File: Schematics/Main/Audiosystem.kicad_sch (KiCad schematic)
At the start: 2 parts

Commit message: Added potentiometer and loudspeakers to audio schematic
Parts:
- added RV1: 2 kΩ, symbol Device:R_Potentiometer_Dual
- R10, R11: value 1 MΩ -> 220 kΩ
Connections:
- net LOUT-: now also RV1.6
- net ROUT-: now also RV1.1
- new net PAM8403-Board/LOUT-: RV1.4
- new net PAM8403-Board/ROUT-: RV1.3
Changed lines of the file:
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@@
 	(wire
 		(pts
-			(xy 176.53 114.3) (xy 186.69 114.3)
+			(xy 203.2 102.87) (xy 215.9 102.87)
 		)
 		(stroke
@@
 	(wire
 		(pts
+			(xy 203.2 114.3) (xy 176.53 114.3)
+		)
+		(stroke
+			(width 0)
+			(type default)
+		)
+	)
+	(wire
+		(pts
+			(xy 187.96 123.19) (xy 187.96 125.73)
+		)
+		(stroke
+			(width 0)
+			(type default)
+		)
+	)
+	(wire
+		(pts
 			(xy 105.41 107.95) (xy 105.41 104.14)
 		)
@@
 	(wire
 		(pts
+			(xy 205.74 135.89) (xy 215.9 135.89)
+		)
+		(stroke
+			(width 0)
+			(type default)
+		)
+	)
+	(wire
+		(pts
 			(xy 143.51 114.3) (xy 148.59 114.3)
 		)
@@
 	(wire
 		(pts
-			(xy 176.53 116.84) (xy 186.69 116.84)
-		)
-		(stroke
-			(width 0)
-			(type default)
-		)
-	)
-	(wire
-		(pts
 			(xy 100.33 104.14) (xy 97.79 104.14)
 		)
@@
 	(wire
 		(pts
+			(xy 187.96 125.73) (xy 176.53 125.73)
+		)
+		(stroke
+			(width 0)
+			(type default)
+		)
+	)
+	(wire
+		(pts
 			(xy 76.2 127) (xy 80.01 127)
 		)
@@
 	(wire
 		(pts
+			(xy 205.74 110.49) (xy 205.74 106.68)
+		)
+		(stroke
+			(width 0)
+			(type default)
+		)
+	)
+	(wire
+		(pts
+			(xy 205.74 130.81) (xy 205.74 135.89)
+		)
+		(stroke
+			(width 0)
+			(type default)
+		)
+	)
+	(wire
+		(pts
+			(xy 203.2 139.7) (xy 203.2 128.27)
+		)
+		(stroke
+			(width 0)
+			(type default)
+		)
+	)
+	(wire
+		(pts
 			(xy 100.33 101.6) (xy 100.33 104.14)
 		)
@@
 	(wire
 		(pts
+			(xy 203.2 128.27) (xy 176.53 128.27)
+		)
+		(stroke
+			(width 0)
+			(type default)
+		)
+	)
+	(wire
+		(pts
+			(xy 205.74 123.19) (xy 187.96 123.19)
+		)
+		(stroke
+			(width 0)
+			(type default)
+		)
+	)
+	(wire
+		(pts
 			(xy 62.23 119.38) (xy 80.01 119.38)
 		)
@@
 	(wire
 		(pts
+			(xy 203.2 102.87) (xy 203.2 114.3)
+		)
+		(stroke
+			(width 0)
+			(type default)
+		)
+	)
+	(wire
+		(pts
 			(xy 62.23 114.3) (xy 80.01 114.3)
 		)
@@
 	(wire
 		(pts
-			(xy 176.53 128.27) (xy 186.69 128.27)
+			(xy 203.2 139.7) (xy 215.9 139.7)
 		)
 		(stroke
@@
 	(wire
 		(pts
-			(xy 176.53 125.73) (xy 186.69 125.73)
-		)
-		(stroke
-			(width 0)
-			(type default)
-		)
-	)
-	(wire
-		(pts
 			(xy 137.16 128.27) (xy 148.59 128.27)
 		)
@@
 	(wire
 		(pts
+			(xy 187.96 116.84) (xy 176.53 116.84)
+		)
+		(stroke
+			(width 0)
+			(type default)
+		)
+	)
+	(wire
+		(pts
+			(xy 187.96 118.11) (xy 205.74 118.11)
+		)
+		(stroke
+			(width 0)
+			(type default)
+		)
+	)
+	(wire
+		(pts
 			(xy 60.96 92.71) (xy 66.04 92.71)
 		)
@@
 	(wire
 		(pts
+			(xy 205.74 106.68) (xy 215.9 106.68)
+		)
+		(stroke
+			(width 0)
+			(type default)
+		)
+	)
+	(wire
+		(pts
 			(xy 76.2 121.92) (xy 80.01 121.92)
+		)
+		(stroke
+			(width 0)
+			(type default)
+		)
+	)
+	(wire
+		(pts
+			(xy 187.96 118.11) (xy 187.96 116.84)
 		)
 		(stroke
@@
 	(hierarchical_label "ROUT-"
 		(shape output)
-		(at 186.69 116.84 0)
+		(at 215.9 106.68 0)
 		(effects
 			(font
@@
 	(hierarchical_label "LOUT+"
 		(shape output)
-		(at 186.69 128.27 0)
+		(at 215.9 139.7 0)
 		(effects
 			(font
@@
 	(hierarchical_label "LOUT-"
 		(shape output)
-		(at 186.69 125.73 0)
+		(at 215.9 135.89 0)
 		(effects
 			(font
@@
 	(hierarchical_label "ROUT+"
 		(shape output)
-		(at 186.69 114.3 0)
+		(at 215.9 102.87 0)
 		(effects
 			(font
@@
 			)
 		)
-		(property "Value" "1 MΩ"
+		(property "Value" "220 kΩ"
 			(at 133.35 119.38 90)
 			(effects
@@
 				(path "/2b6c83b8-b6db-46e9-a845-f7ffa0649aa2/64921ae5-eabb-49e5-933f-c558e83970f3"
 					(reference "#PWR042")
+					(unit 1)
+				)
+			)
+		)
+	)
+	(symbol
+		(lib_id "Device:R_Potentiometer_Dual")
+		(at 208.28 120.65 270)
+		(unit 1)
+		(exclude_from_sim no)
+		(in_bom yes)
+		(on_board yes)
+		(dnp no)
+		(fields_autoplaced yes)
+		(property "Reference" "RV1"
+			(at 203.2 119.3799 90)
+			(effects
+				(font
+					(size 1.27 1.27)
+				)
+				(justify right)
+			)
+		)
+		(property "Value" "2 kΩ"
+			(at 203.2 121.9199 90)
+			(effects
+				(font
+					(size 1.27 1.27)
+				)
+				(justify right)
+			)
+		)
+		(property "Footprint" ""
+			(at 206.375 127 0)
+			(effects
+				(font
+					(size 1.27 1.27)
+				)
+				(hide yes)
+			)
+		)
+		(property "Datasheet" "~"
+			(at 206.375 127 0)
+			(effects
+				(font
+					(size 1.27 1.27)
+				)
+				(hide yes)
+			)
+		)
+		(property "Description" "Dual potentiometer"
+			(at 208.28 120.65 0)
+			(effects
+				(font
+					(size 1.27 1.27)
+				)
+				(hide yes)
+			)
+		)
+		(pin "4"
+		)
+		(pin "3"
+		)
+		(pin "1"
+		)
+		(pin "5"
+		)
+		(pin "2"
+		)
+		(pin "6"
+		)
+		(instances
+			(project ""
+				(path "/2b6c83b8-b6db-46e9-a845-f7ffa0649aa2/64921ae5-eabb-49e5-933f-c558e83970f3"
+					(reference "RV1")
 					(unit 1)
 				)
@@
 			)
 		)
-		(property "Value" "1 MΩ"
+		(property "Value" "220 kΩ"
 			(at 133.35 132.08 90)
 			(effects

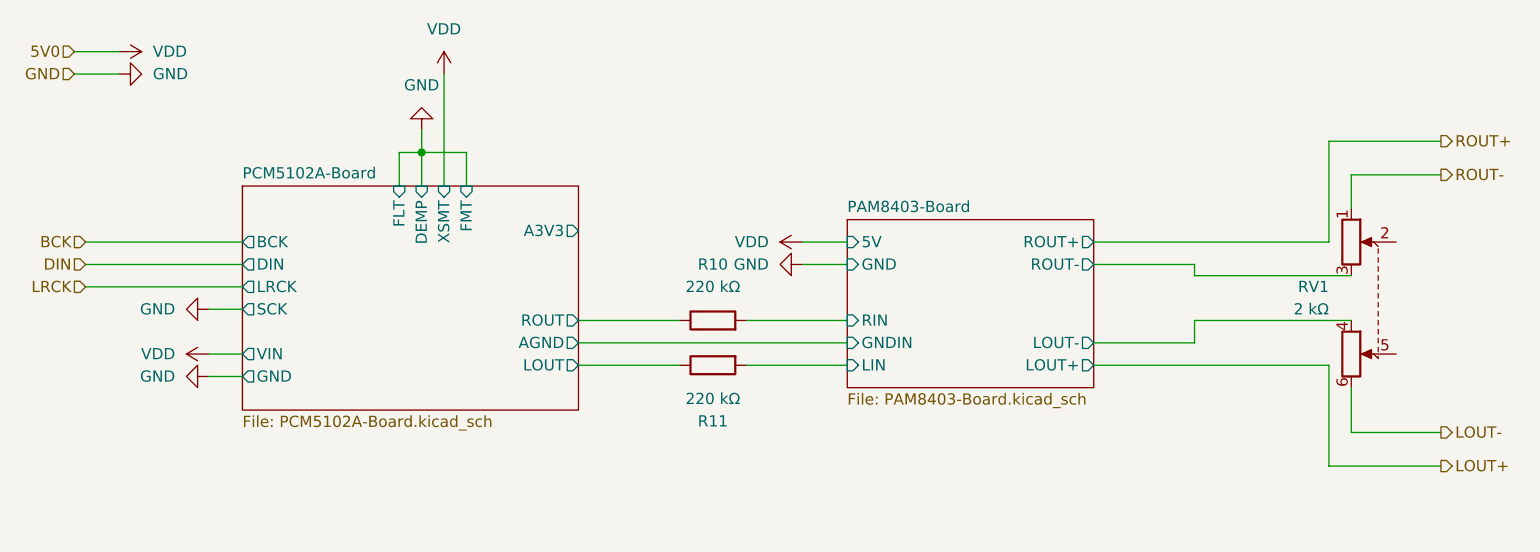
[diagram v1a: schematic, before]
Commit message: Corrected poti position in schematic
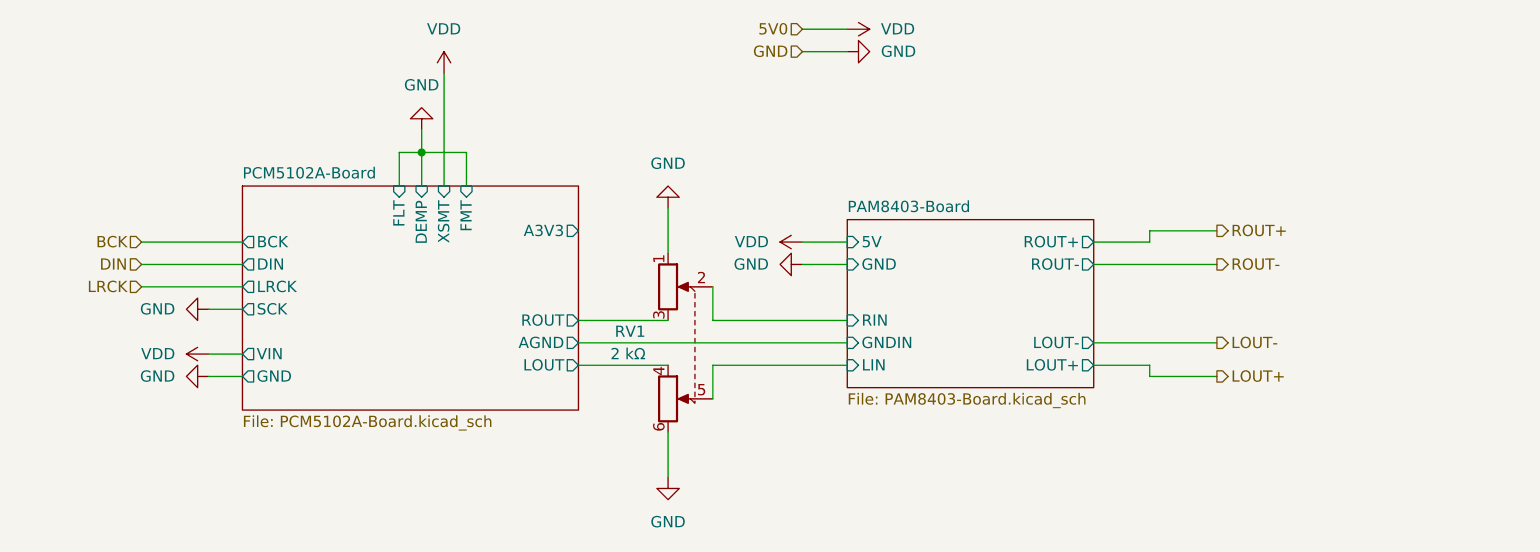
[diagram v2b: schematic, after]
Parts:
- removed R10, R11: 220 kΩ, symbol Device:R
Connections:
- net PAM8403-Board/LOUT- is gone; now on net PCM5102A-Board/LOUT: RV1.4
- net PAM8403-Board/ROUT- is gone; now on net PCM5102A-Board/ROUT: RV1.3
- net GND: now also RV1.1, RV1.6
- net LOUT-: no longer RV1.6
- net PAM8403-Board/LIN: now also RV1.5
- net PAM8403-Board/RIN: now also RV1.2
- net ROUT-: no longer RV1.1
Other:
- moved on the sheet: RV1
